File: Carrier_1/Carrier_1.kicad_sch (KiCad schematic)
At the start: 9 parts, among them J1 CH1, J2 HV, J3 CH2, J4 GND, U1 LGAD_2_pad

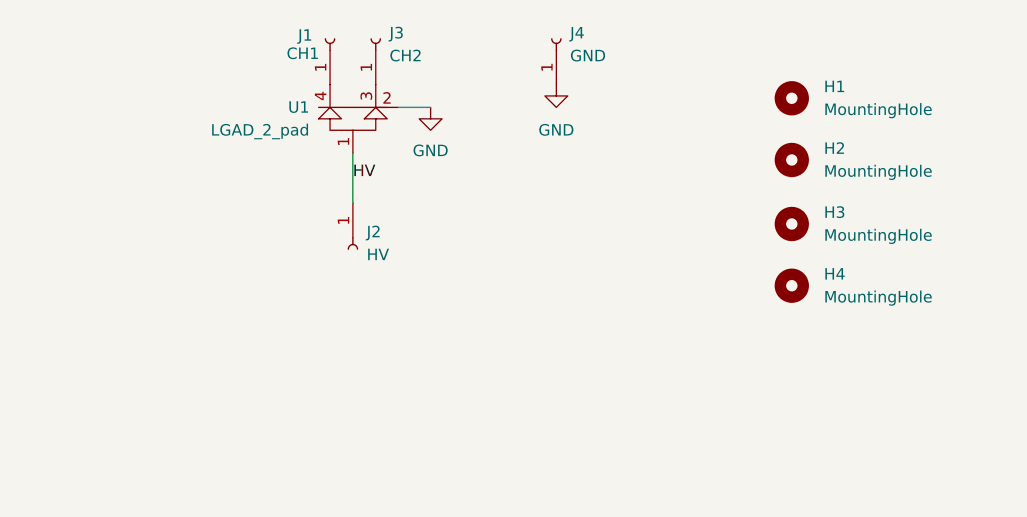
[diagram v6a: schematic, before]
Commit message: Prototype with 4 channels
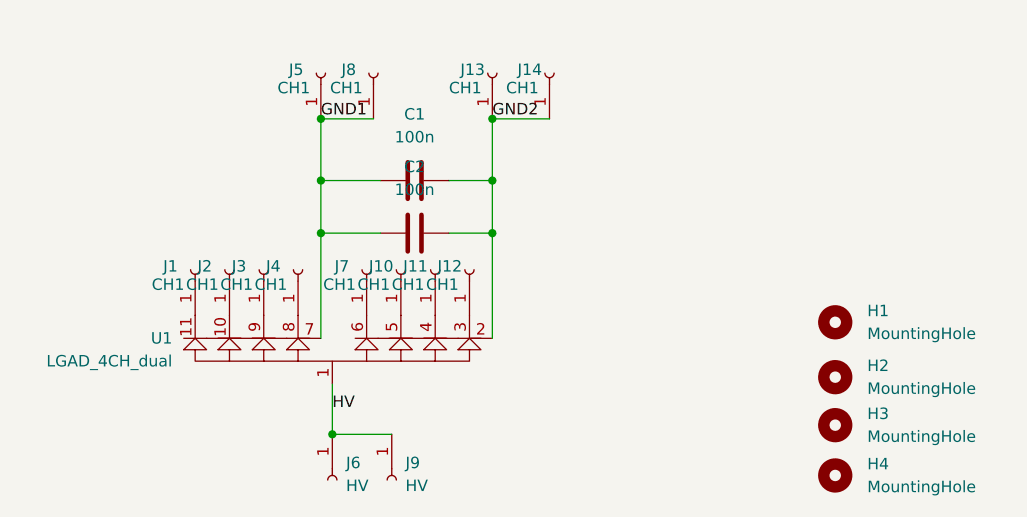
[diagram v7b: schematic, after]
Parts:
- removed U1: LGAD_2_pad, chubut:LGAD, symbol LGAD:LGAD_2_pad
- added C1, C2: 100n, Capacitor_SMD:C_0805_2012Metric, symbol Device:C
- added J1, J10, J11, J13, J14, J2, J5, J7, J8: CH1, chubut:MILL-MAX_0965-0-15-20-80-14-11-0_contact, symbol Connector:Conn_01x01_Female
- added J9: HV, chubut:MILL-MAX_0965-0-15-20-80-14-11-0_contact, symbol Connector:Conn_01x01_Female
- added U1: LGAD_4CH_dual, chubut:LGAD_4CH_dual, symbol LGAD:LGAD_4CH_dual
- H1, H2, H3, H4: footprint MountingHole:MountingHole_2.1mm -> chubut:MILL-MAX_0965-0-15-20-80-14-11-0_alignment_hole
- J3: value CH2 -> CH1
- J4: value GND -> CH1
- renumbered J1 to J12, J2 to J6
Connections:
- net HV: now also J9.1 (Pin_1), U1.1
- net at J3.1 (Pin_1): now also U1.9
- net at J12.1 (Pin_1): now also U1.3
- net GND: no longer names the net of J4.1 (Pin_1)
- net GND: now also U1.8
- new net: J1.1 (Pin_1), U1.11
- new net: J2.1 (Pin_1), U1.10
- new net: J11.1 (Pin_1), U1.4
- new net: J10.1 (Pin_1), U1.5
- new net: J7.1 (Pin_1), U1.6
- new net GND1: C1.1, C2.1, J5.1 (Pin_1), J8.1 (Pin_1), U1.7
- new net GND2: C1.2, C2.2, J13.1 (Pin_1), J14.1 (Pin_1), U1.2
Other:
- moved on the sheet: H1, J12, J6

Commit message: Updated carrier for new design
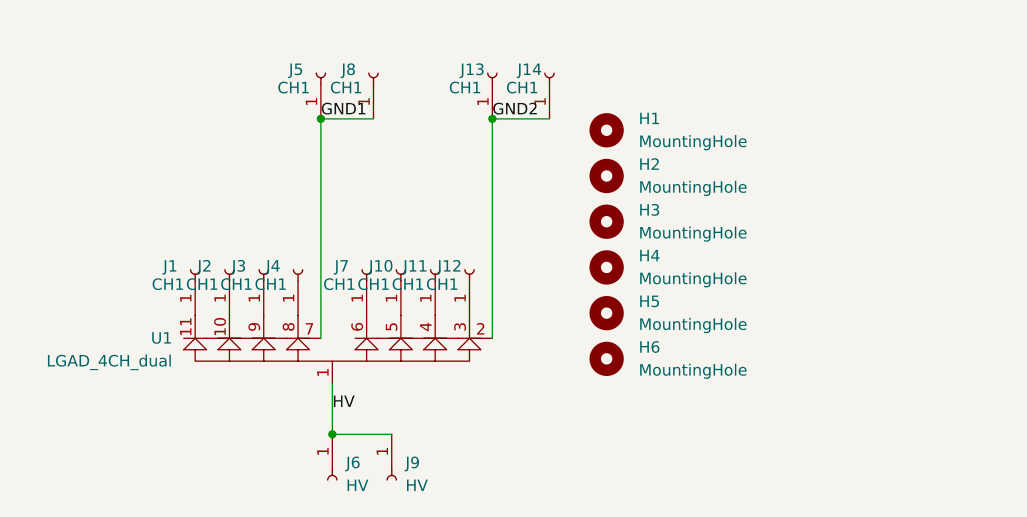
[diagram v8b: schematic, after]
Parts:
- removed C1, C2: 100n, Capacitor_SMD:C_0805_2012Metric, symbol Device:C
- added H5, H6: MountingHole, chubut:MILL-MAX_7625-0-00-15-00-00-03-0_alignment_hole, symbol Mechanical:MountingHole
- H1, H2, H3, H4: footprint chubut:MILL-MAX_0965-0-15-20-80-14-11-0_alignment_hole -> chubut:MILL-MAX_7625-0-00-15-00-00-03-0_alignment_hole
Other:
- moved on the sheet: H1, H2, H3, H4
